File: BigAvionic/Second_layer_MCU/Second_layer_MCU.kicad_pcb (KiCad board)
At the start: 4 copper layers, 68 x 68 mm, 98 parts, among them J1 Conn_01x04, J10 Conn_01x04, J11 Conn_01x04, J13 Conn_01x08, J14 Conn_01x08, J2 USB_C_Receptacle_USB2.0_16P, J3 Conn_01x02, J4 Micro_SD_Card_Det1, J5 Conn_01x04, J6 Conn_01x04, J7 Screw_Terminal_01x02, J8 Conn_01x04, J9 Conn_01x08, Q2 BSS138, SW1 SW_Push, SW2 SW_Push_Shielded, SW3 SW_Push_Shielded, U1 STM32F405VGTx, U2 W25Q128JVS, U3 ADXL375BCCZ, U4 BMP390, U5 BMI088, Y1 FA-238 16Mhz

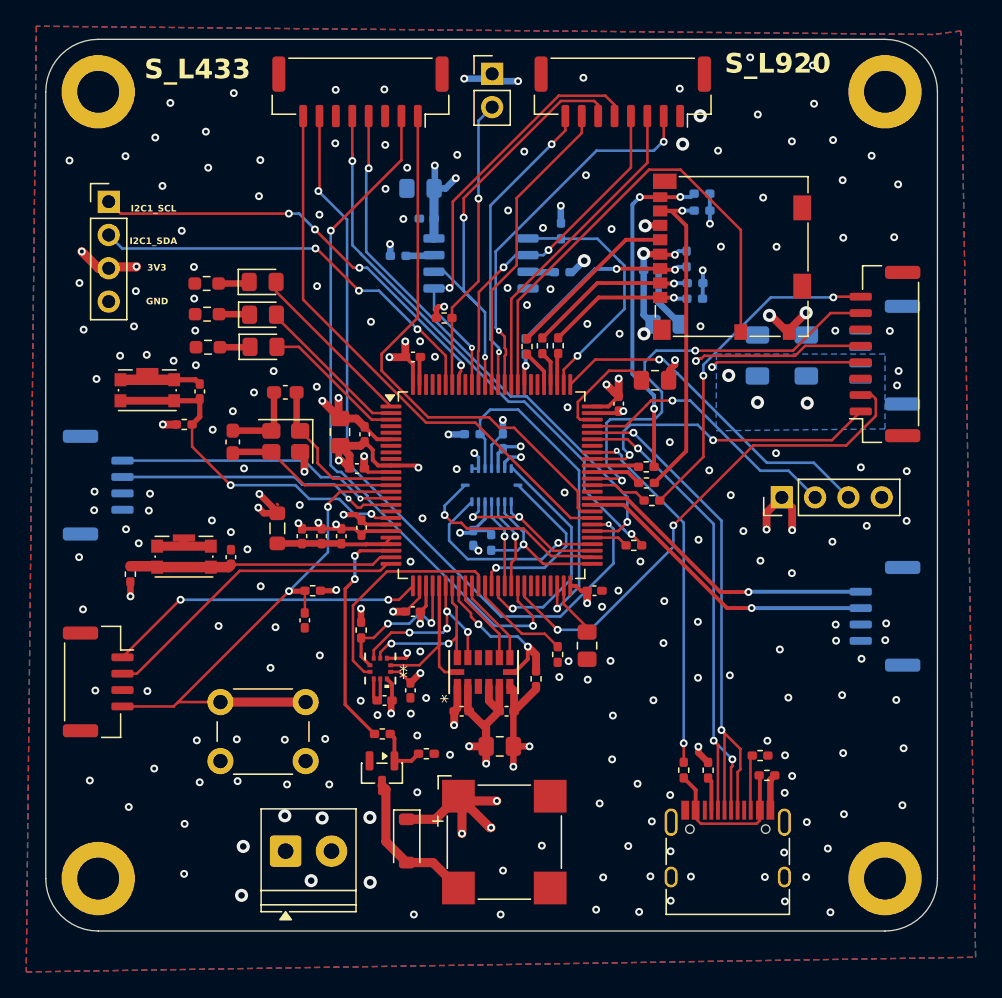
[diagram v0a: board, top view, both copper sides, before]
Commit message: edit some in MCU for production
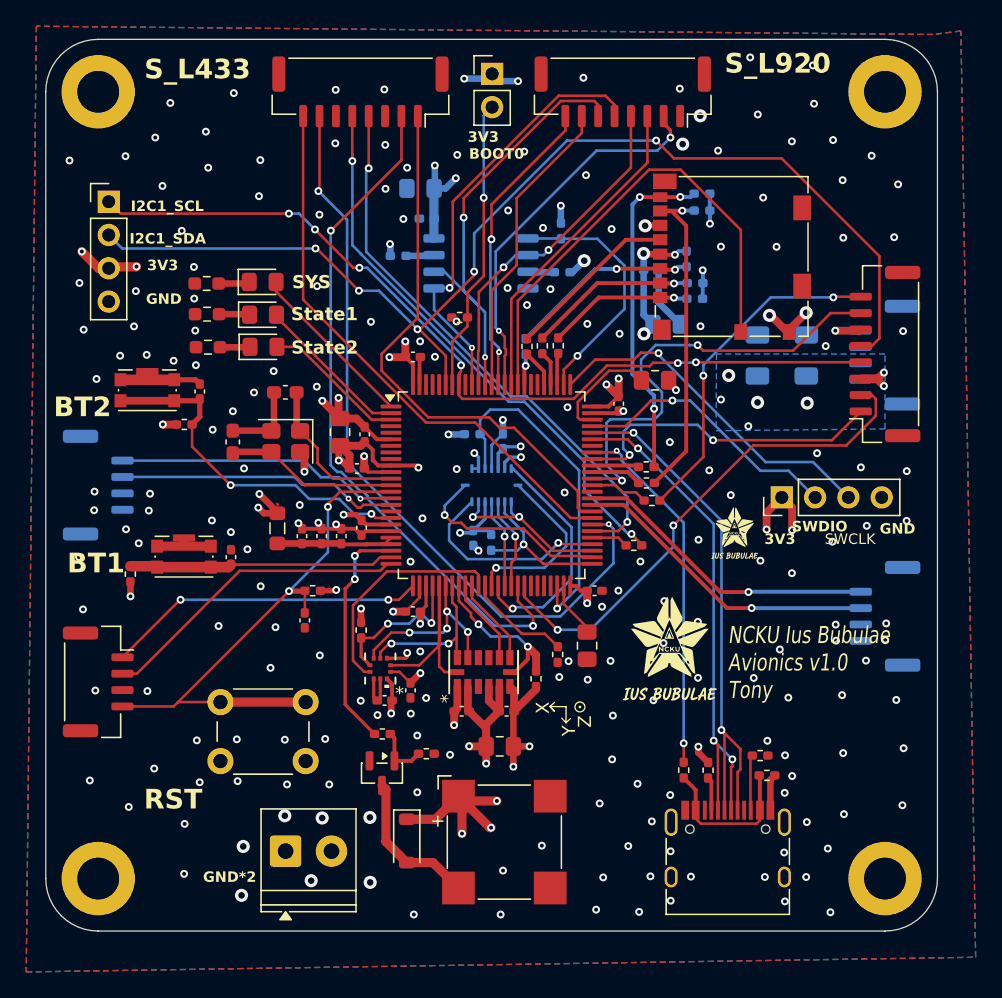
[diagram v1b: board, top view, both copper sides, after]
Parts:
- added G***: LOGO, Lib:LOGO-10*12.1, F.Cu at (144.1, 132.8)
- added G***: LOGO, Lib:Untitled, F.Cu at (149.0, 123.8)
- moved R16 1.18 mm to (128.1, 107.2)
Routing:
- net I2C1_SDA: track 67.0 -> 86.3 mm, vias 4 -> 5
- net GND: track 92.6 -> 96.4 mm, vias 217 -> 220
- net I2C1_SCL: track 64.8 -> 66.5 mm, vias 5 -> 6
- net UART6_RX: track 34.2 -> 35.0 mm
- net LORA920_RST: track 28.8 -> 29.3 mm
- net SWCLK: track 26.4 -> 26.9 mm
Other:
- board text added: "BOOT0"
- board text added: "BT1"
- board text added: "BT2"
- board text added: "GND*2"
- board text added: "Ignition"
- board text added: "NCKU Ius Bubulae Avionics v1.0 Tony"
- board text added: "RST"
- board text added: "SWCLK"
- board text added: "SWDIO"
- board text added: "SYS"
- board text added: "State1"
- board text added: "State2"

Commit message: version for v1 production
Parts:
- removed the G*** at (149.0, 123.8)
- C17, C18: value 15pF -> 10pF
- D1: value G -> Y
- D2: value R -> G
- D3: value B -> W
- Q2: value BSS138 -> AO3400A
- R27: value 2.2k -> 220
- R28, R29: value 2.2k -> 100
- U4: value BMP390 -> BMP388/390
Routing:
- net +3.3V: track 122.4 -> 120.9 mm
- net UART3_RX: track 43.0 -> 42.4 mm
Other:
- board text added: "MCU Layey"
- board text added: "S_POWER"
- board text added: "S_TOP"
